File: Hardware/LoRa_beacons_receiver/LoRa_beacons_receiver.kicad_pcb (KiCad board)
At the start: 2 copper layers, 62.5 x 49 mm, 37 parts, among them J1 Conn_Coaxial, J2 USB_C_Receptacle_USB2.0_16P, J3 I2C_Display, J4 ST-Link, J5 1PPS_out, J6 Conn_02x09_Counter_Clockwise, Q1 DMG3402L, Q2 DMG3402L, SW1 RST_button, SW2 BOOT_button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

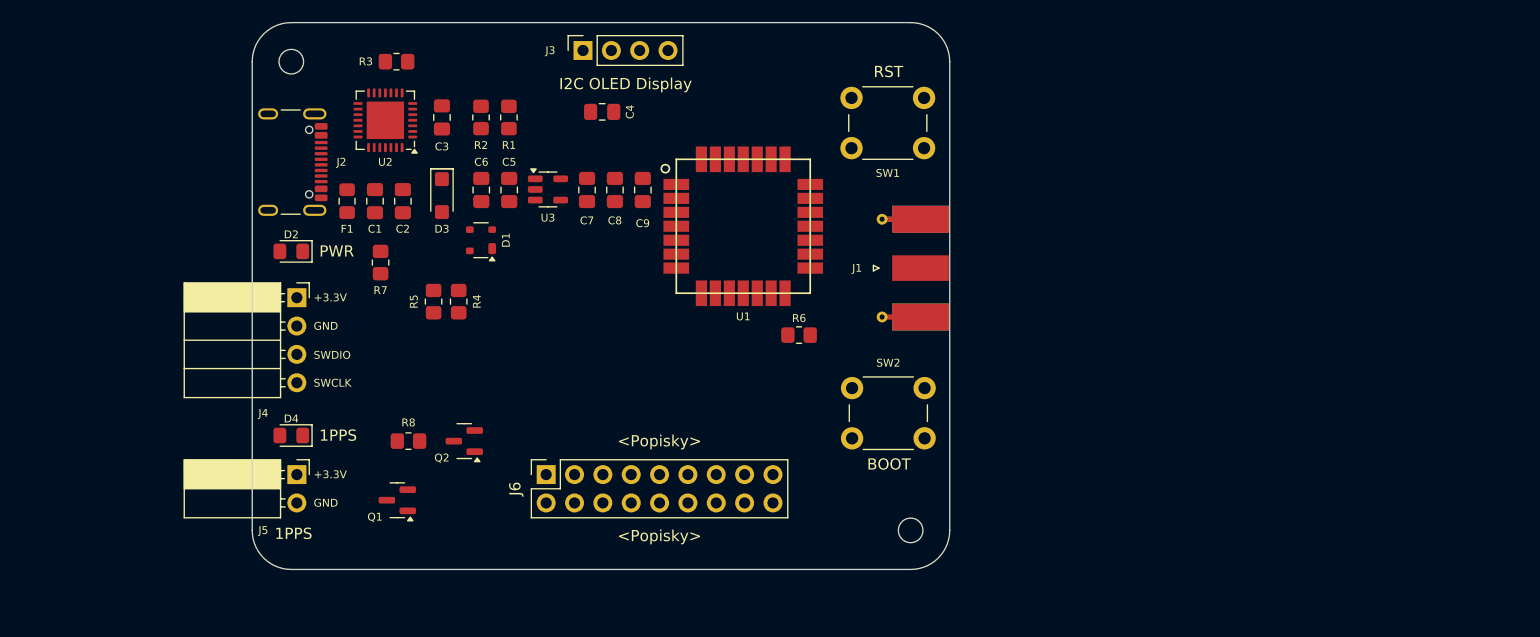
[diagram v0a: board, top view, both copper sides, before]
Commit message: Recommended KiCAD changes; PCB layout changes
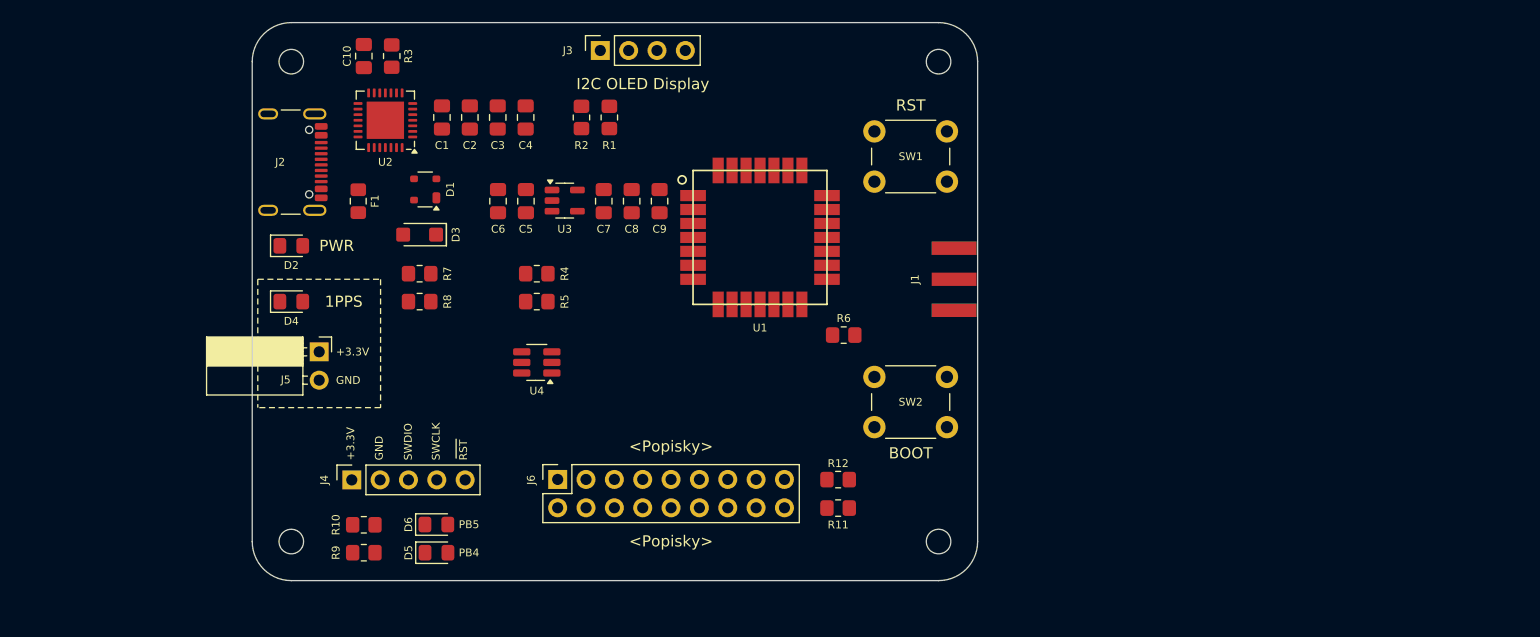
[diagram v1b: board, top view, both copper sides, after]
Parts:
- removed Q1, Q2: DMG3402L, Package_TO_SOT_SMD:SOT-23
- added C10: 100n, Capacitor_SMD:C_0805_2012Metric_Pad1.18x1.45mm_HandSolder, F.Cu at (110.0, 54.0)
- added D5: PB4, LED_SMD:LED_0805_2012Metric_Pad1.15x1.40mm_HandSolder, F.Cu at (116.5, 98.5)
- added D6: PB5, LED_SMD:LED_0805_2012Metric_Pad1.15x1.40mm_HandSolder, F.Cu at (116.5, 96.0)
- added H3: MountingHole, MountingHole:MountingHole_2.2mm_M2, F.Cu at (103.5, 97.5)
- added H4: MountingHole, MountingHole:MountingHole_2.2mm_M2, F.Cu at (161.5, 54.5)
- added R10: 56R, Resistor_SMD:R_0805_2012Metric_Pad1.20x1.40mm_HandSolder, F.Cu at (110.0, 96.0)
- added R11: 4.7k, Resistor_SMD:R_0805_2012Metric_Pad1.20x1.40mm_HandSolder, F.Cu at (152.5, 94.5)
- added R12: 4.7k, Resistor_SMD:R_0805_2012Metric_Pad1.20x1.40mm_HandSolder, F.Cu at (152.5, 92.0)
- added R9: 56R, Resistor_SMD:R_0805_2012Metric_Pad1.20x1.40mm_HandSolder, F.Cu at (110.0, 98.5)
- added U4: 74LVC1G175, Package_TO_SOT_SMD:SOT-23-6_Handsoldering, F.Cu at (125.5, 81.5)
- C1: value 1u -> 4.7u
- C2: value 100n -> 1u
- J1: footprint Connector_Coaxial:SMA_Molex_73251-1153_EdgeMount_Horizontal -> Connector_Coaxial_g:RF2-143-T-17-50-G
- J4: footprint Connector_PinSocket_2.54mm:PinSocket_1x04_P2.54mm_Horizontal -> Connector_PinSocket_2.54mm:PinSocket_1x05_P2.54mm_Vertical
- moved J4 17.1 mm to (108.9, 92.0), turned to 90 degrees
- moved R8 12.5 mm to (115.0, 76.0), turned to 180 degrees
- moved D4 12.0 mm to (103.5, 76.0), turned to 0 degrees
- moved SW1 11.4 mm to (162.2, 65.2), turned to 180 degrees
- moved J5 11.2 mm to (106.0, 80.5)
- moved C1 9.60 mm to (117.0, 59.5)
- moved C2 9.60 mm to (119.5, 59.5), turned to -90 degrees
- moved R5 9.25 mm to (125.5, 76.0), turned to 180 degrees
- moved R1 9.00 mm to (132.0, 59.5)
- moved R2 9.00 mm to (129.5, 59.5)
- moved R4 7.43 mm to (125.5, 73.5), turned to 0 degrees
- moved C4 6.88 mm to (124.5, 59.5), turned to -90 degrees
- moved J1 6.81 mm to (164.9, 74.0), turned to 90 degrees
- moved D1 6.76 mm to (115.5, 66.0)
- moved C3 5.00 mm to (122.0, 59.5)
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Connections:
- C1 pad 1: +5V -> GND
- C1 pad 2: GND -> +3.3V
- C2 pad 1: +5V -> +3.3V
- C3 pad 1: VDD -> +3.3V
- C4 pad 1: //DTR -> +3.3V
- C4 pad 2: RST -> GND
- D2 pad 1: /PWR_LED -> GND
- D2 pad 2: +3.3V -> /PWR_LED_A
- D4 pad 1: /PPS_LED -> GND
- D4 pad 2: +3.3V -> /PPS_LED_A
- J5 pad 1: +3.3V -> /PPS_OUT
- J5 pad 2: /PPS_OUT_MOS_D -> GND
- R3 pad 1: VDD -> +3.3V
- R3 pad 2: /USB-UART_RST -> /RST
- R7 pad 1: /PWR_LED -> +3.3V
- R7 pad 2: GND -> /PWR_LED_A
- R8 pad 1: /PPS_LED -> 1PPS_LED
- R8 pad 2: /PPS_LED_MOS_D -> /PPS_LED_A
- SW1 pad 1: RST -> /RST
- U1 pad 17: RST -> /RST
- U1 pad 23: 1PPS_OUT -> 1PPS_CLK
- U2 pad 6: VDD -> +3.3V
- U2 pad 7: +5V -> +3.3V
- U2 pad 9: /USB-UART_RST -> /RST
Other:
- board size 62.5 x 49 mm -> 65 x 50 mm
- board text added: "PB4"
- board text added: "PB5"

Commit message: Clenaup
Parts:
- J1: footprint Connector_Coaxial_g:RF2-143-T-17-50-G -> Connector_Coaxial_l:RF2-143-T-17-50-G_l
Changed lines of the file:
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@@
 		)
 		(embedded_fonts no)
-		(model "${KIPRJMOD}/symbols/STM32_module_l.pretty/STM32WLE5JC_3D.stp"
+		(model "${KIPRJMOD}/3dmodels/STM32WLE5JC_3D_l.stp"
 			(offset
 				(xyz 0 0 2.5)
 			)
 			(scale
-				(xyz 0.0385 0.0385 0.0385)
+				(xyz 0.0395 0.0395 0.0395)
 			)
 			(rotate
@@
 		)
 		(embedded_fonts no)
-		(model "${KIPRJMOD}/symbols/Diode_SMD_l.pretty/MBR130LSFT1G.stp"
+		(model "${KIPRJMOD}/3dmodels/MBR130LSFT1G_l.stp"
 			(offset
 				(xyz 0 0 0)
@@
 			)
 		)
-		(model "${KIPRJMOD}/symbols/Display_l.pretty/OLED_0_96INCH.step"
+		(model "${KIPRJMOD}/3dmodels/OLED_0_96INCH_l.step"
 			(offset
 				(xyz 0 -9.15 11.5)
@@
 		)
 	)
-	(footprint "Connector_Coaxial_g:RF2-143-T-17-50-G"
+	(footprint "Connector_Coaxial_l:RF2-143-T-17-50-G_l"
 		(layer "F.Cu")
 		(at 164.9 74 90)
 		(property "Reference" "J1"
-			(at 0 -5.5066 90)
+			(at -0.325 -6.635 90)
 			(layer "F.SilkS")
 			(effects
 				(font
-					(size 0.7 0.7)
-					(thickness 0.1)
+					(size 1 1)
+					(thickness 0.15)
 				)
 			)
@@
 		)
 		(embedded_fonts no)
-		(model "C:/Users/DELL_KM/Documents/KiCad/9.0/3dmodels/RF2-143-T-17-50-G.step"
+		(model "${KIPRJMOD}/3dmodels/RF2-143-T-17-50-G_l.step"
 			(offset
 				(xyz 0 0 0)

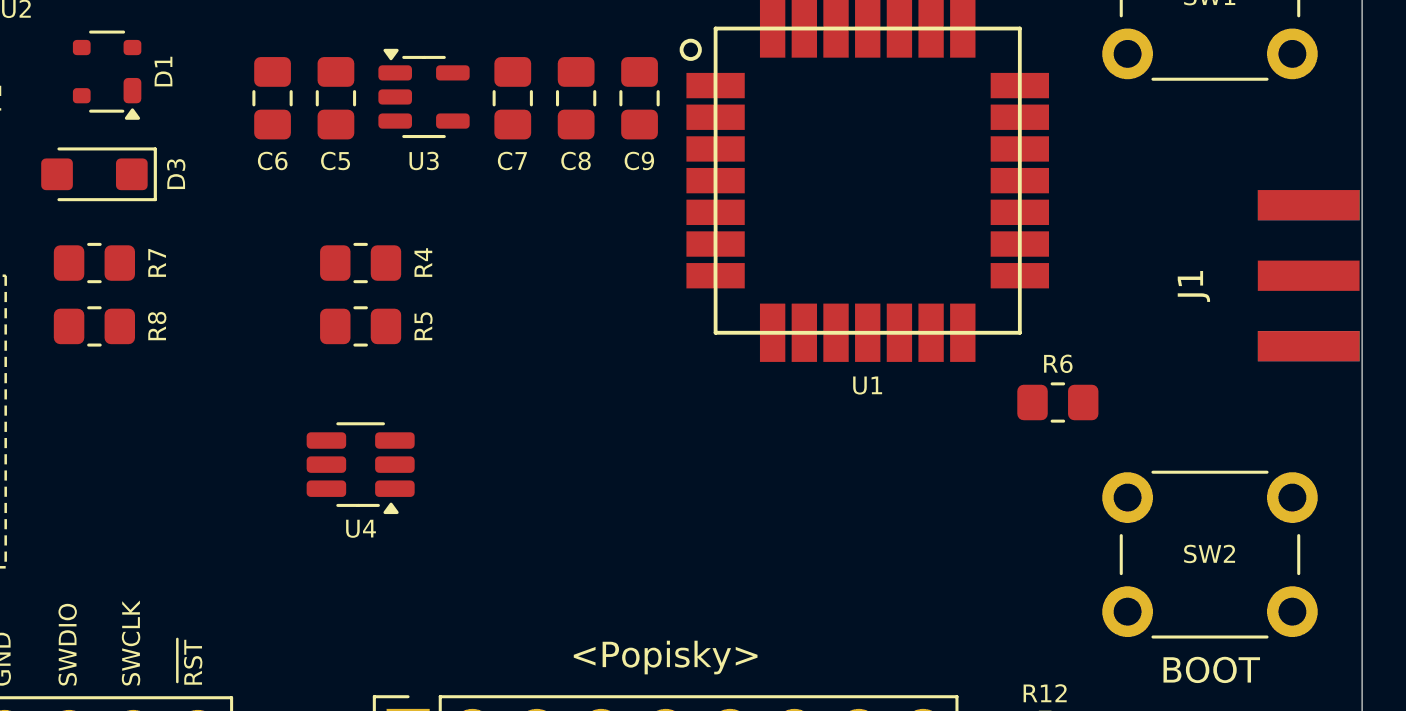
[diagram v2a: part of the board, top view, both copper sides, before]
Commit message: Minor schematic changes
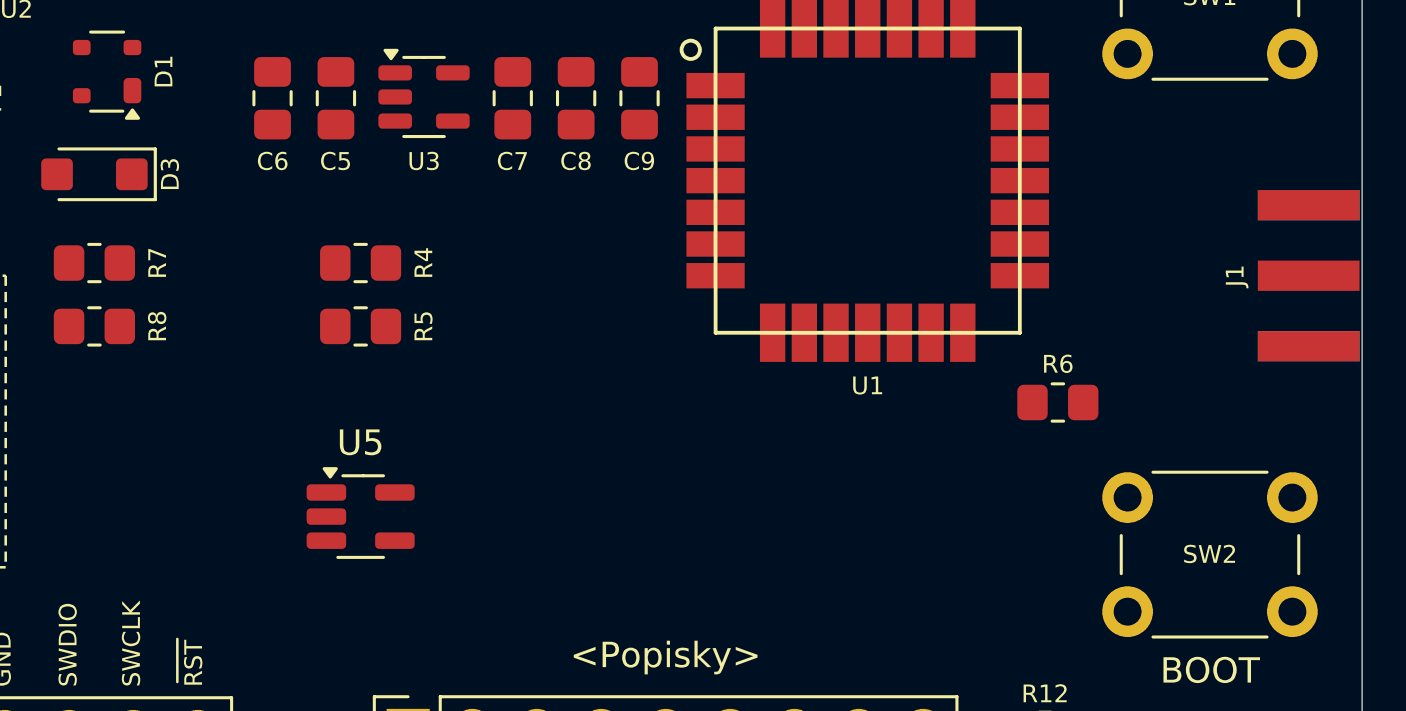
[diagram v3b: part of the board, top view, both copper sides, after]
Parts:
- removed U4: 74LVC1G175, Package_TO_SOT_SMD:SOT-23-6_Handsoldering
- added U5: 74LVC1G17, Package_TO_SOT_SMD:SOT-23-5_HandSoldering, F.Cu at (125.5, 83.5)
- D3: footprint Diode_SMD_l:SOD-123FL -> Diode_SMD_l:SOD-123FL_l
- U1: footprint STM32_module_l:STM32WLE5JC -> STM32_module_l:STM32WLE5JC_l
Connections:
- J6 pad 9: GND -> PB3
- R8 pad 1: 1PPS_LED -> /PPS_LED_A
- R8 pad 2: /PPS_LED_A -> 1PPS_CLK
- U1 pad 8: 1PPS_LED -> PB3

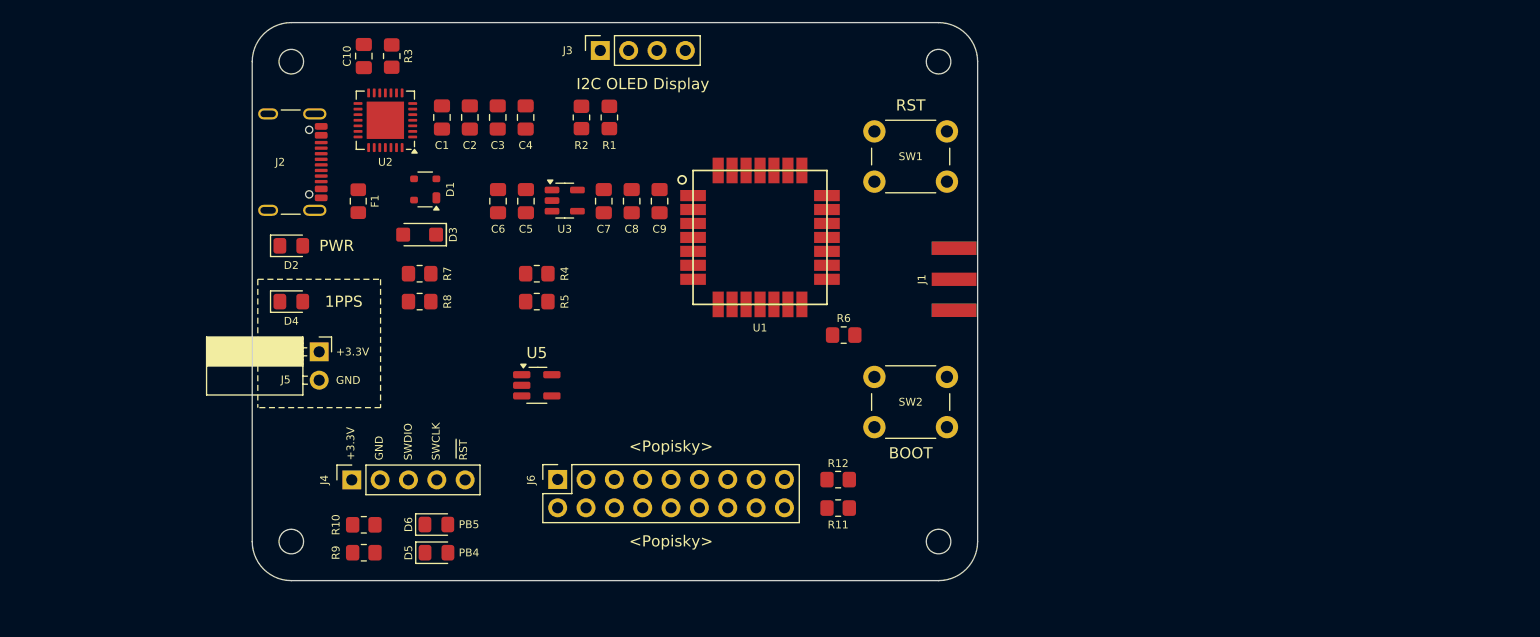
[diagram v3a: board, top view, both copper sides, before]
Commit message: Minor schematic changes; PCB WIP
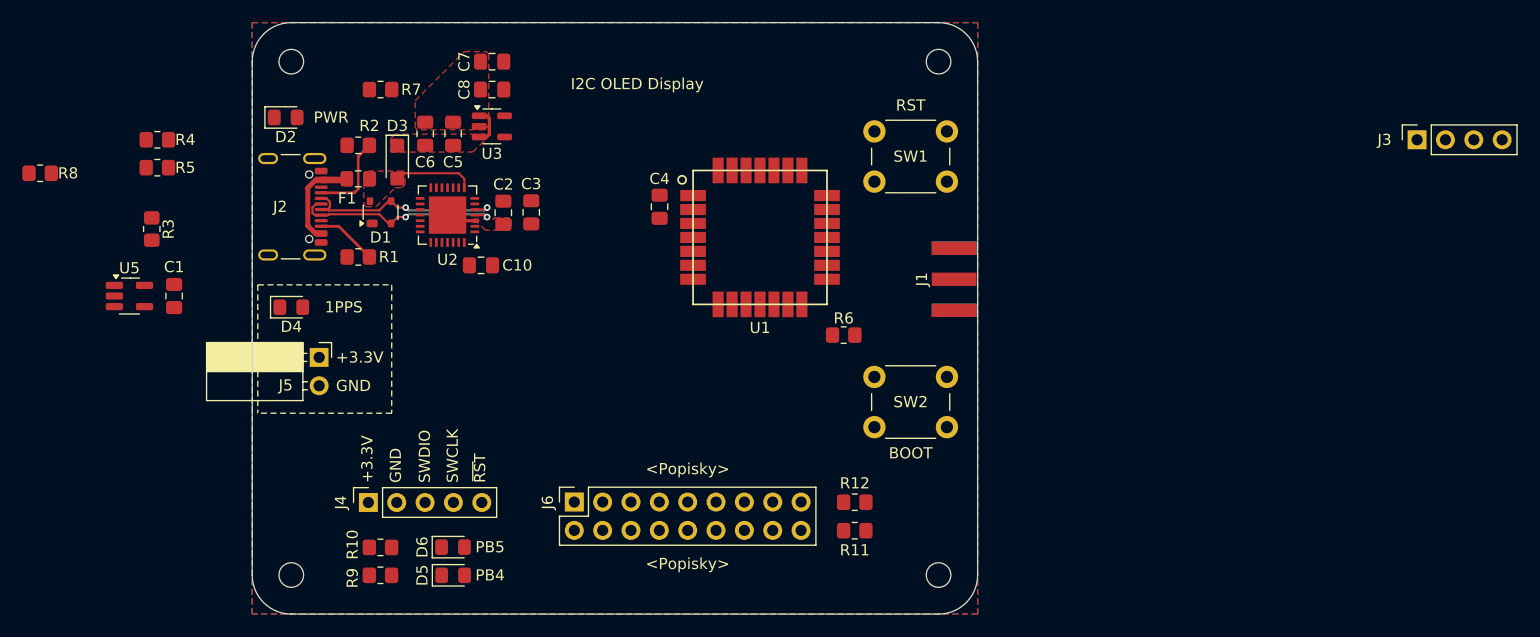
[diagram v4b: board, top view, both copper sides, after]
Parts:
- removed C9: 4.7u, Capacitor_SMD:C_0805_2012Metric_Pad1.18x1.45mm_HandSolder
- C1: value 4.7u -> 100n
- C4: value 100n -> 4.7u
- U1: value STM32WLE5JC -> Wio-E5
- moved J3 73.6 mm to (208.2, 61.5)
- moved U5 37.4 mm to (89.0, 75.5)
- moved R4 36.1 mm to (91.5, 61.5)
- moved R5 36.1 mm to (91.5, 64.0)
- moved R8 35.9 mm to (81.0, 64.5), turned to 0 degrees
- moved C1 28.8 mm to (93.0, 75.5), turned to -90 degrees
- moved R3 26.5 mm to (91.0, 69.5)
- moved R1 25.7 mm to (109.5, 72.0), turned to 180 degrees
- moved C10 21.5 mm to (120.5, 72.8), turned to 0 degrees
- moved R2 20.2 mm to (109.5, 62.0), turned to 180 degrees
- moved R7 16.9 mm to (111.5, 57.0)
- moved C7 16.0 mm to (121.5, 54.5), turned to 180 degrees
- moved C8 16.0 mm to (121.5, 57.0), turned to 180 degrees
- moved C4 14.4 mm to (136.5, 67.5)
- moved D2 11.5 mm to (103.0, 59.5)
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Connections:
- net /D+ renamed /USB_D_P
- net /D- renamed /USB_D_N
- C1 pad 1: GND -> +3.3V
- C1 pad 2: +3.3V -> GND
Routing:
- net /USB_D_N: track 0.00 -> 19.1 mm, vias 0 -> 2
- net /USB_D_P: track 0.00 -> 19.1 mm, vias 0 -> 2
- net /VBUS: track 0.00 -> 8.72 mm
- net /CC1: track 0.00 -> 7.78 mm
- net +5V: track 0.00 -> 7.24 mm
- net /CC2: track 0.00 -> 5.46 mm
- net /LDO_VIN: track 0.00 -> 3.43 mm
- net GND: track 0.00 -> 2.66 mm
- added copper zone on F.Cu, net +3.3V
- added copper zone on F.Cu, net +5V
- added copper zone on F.Cu, net /LDO_VIN
- added copper zone on B.Cu, net GND
- added copper zone on F.Cu, net GND
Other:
- board size 65 x 50 mm -> 65 x 53 mm

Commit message: First version of completely routed PCB
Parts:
- moved J3 76.1 mm to (132.5, 53.5)
- moved R4 42.2 mm to (129.2, 80.2)
- moved R5 42.0 mm to (129.2, 82.5)
- moved R8 37.5 mm to (116.0, 78.0), turned to -90 degrees
- moved R11 32.3 mm to (129.2, 75.8), turned to 180 degrees
- moved R3 31.1 mm to (121.5, 63.5), turned to 180 degrees
- moved R12 29.4 mm to (129.2, 78.0), turned to 180 degrees
- moved U5 29.2 mm to (117.5, 82.0), turned to 180 degrees
- moved C1 25.6 mm to (116.8, 85.0), turned to 0 degrees
- moved R6 4.07 mm to (150.0, 81.8), turned to 90 degrees
- moved J5 3.00 mm to (109.0, 81.0)
- moved R7 1.50 mm to (111.5, 55.5)
- moved R2 0.50 mm to (109.5, 62.5)
- moved C4 0.40 mm to (136.5, 67.1)
- moved J1 0.10 mm to (164.8, 74.0)
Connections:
- J6 pad 1: +5V -> PB0
- J6 pad 10: GND -> LPUART1_TX
- J6 pad 11: SPI2_MOSI -> SPI2_MISO
- J6 pad 12: SPI2_MISO -> SPI2_MOSI
- J6 pad 13: SPI2_NSS -> SPI2_SCK;BOOT
- J6 pad 14: SPI2_SCK;BOOT -> SPI2_NSS
- J6 pad 15: UART2_TX -> PB10
- J6 pad 16: UART2_RX -> PA9
- J6 pad 17: I2C2_SDA -> UART2_RX
- J6 pad 18: I2C2_SCL -> UART2_TX
- J6 pad 3: PB4 -> I2C2_SCL
- J6 pad 4: PB5 -> I2C2_SDA
- J6 pad 5: PB10 -> PB3
- J6 pad 6: PA9 -> PB4
- J6 pad 7: LPUART1_TX -> PB5
- J6 pad 8: LPUART1_RX -> GND
- J6 pad 9: PB3 -> LPUART1_RX
- U1 pad 28: unconnected-(U1-PB0-Pad28) -> PB0
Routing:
- net /RST: track 0.00 -> 89.2 mm, vias 0 -> 6
- net GND: track 2.66 -> 57.7 mm, vias 0 -> 18
- net I2C2_SDA: track 0.00 -> 52.4 mm, vias 0 -> 2
- net SPI2_SCK;BOOT: track 0.00 -> 51.8 mm, vias 0 -> 1
- net I2C2_SCL: track 0.00 -> 49.6 mm, vias 0 -> 2
- net 1PPS_CLK: track 0.00 -> 49.2 mm, vias 0 -> 2
- net PB4: track 0.00 -> 42.3 mm, vias 0 -> 1
- net SWDIO: track 0.00 -> 42.2 mm, vias 0 -> 1
- net PB5: track 0.00 -> 41.2 mm
- net PB0: track 0.00 -> 39.8 mm, vias 0 -> 1
- net SWCLK: track 0.00 -> 38.6 mm, vias 0 -> 1
- net SPI2_MOSI: track 0.00 -> 34.9 mm, vias 0 -> 1
- net PA9: track 0.00 -> 34.6 mm, vias 0 -> 1
- net SPI2_NSS: track 0.00 -> 33.9 mm, vias 0 -> 1
- net SPI2_MISO: track 0.00 -> 30.9 mm, vias 0 -> 1
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- added copper zone on B.Cu, net +3.3V
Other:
- board text added: "MISO2"
- board text added: "MOSI2"
- board text added: "NSS2"
- board text added: "PA9"
- board text added: "PB0"
- board text added: "PB10"
- board text added: "PB3"
- board text added: "PC0"
- board text added: "PC1"
- board text added: "RX2"
- board text added: "SCK2"
- board text added: "SCL2"
- board text added: "SDA2"
- board text added: "TX2"
- board text removed: "<Popisky>"

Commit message: Minor changes
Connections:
- net UART1_RX-USB renamed UART1_TX-USB_RX
- net UART1_TX-USB renamed UART1_RX-USB_TX
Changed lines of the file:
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@@
 	(net 34 "PB3")
 	(net 35 "1PPS_CLK")
-	(net 36 "UART1_TX-USB")
+	(net 36 "UART1_RX-USB_TX")
 	(net 37 "/TXD")
-	(net 38 "UART1_RX-USB")
+	(net 38 "UART1_TX-USB_RX")
 	(net 39 "/RXD")
 	(net 40 "/BOOT_button")
@@
 			(size 1 2.3)
 			(layers "F.Cu" "F.Mask" "F.Paste")
-			(net 36 "UART1_TX-USB")
+			(net 36 "UART1_RX-USB_TX")
 			(pinfunction "PB7")
 			(pintype "input")
@@
 			(size 1 2.3)
 			(layers "F.Cu" "F.Mask" "F.Paste")
-			(net 38 "UART1_RX-USB")
+			(net 38 "UART1_TX-USB_RX")
 			(pinfunction "PB6")
 			(pintype "input")
@@
 			(layers "F.Cu" "F.Mask" "F.Paste")
 			(roundrect_rratio 0.208333)
-			(net 36 "UART1_TX-USB")
+			(net 36 "UART1_RX-USB_TX")
 			(pintype "passive")
 		)
@@
 			(layers "F.Cu" "F.Mask" "F.Paste")
 			(roundrect_rratio 0.208333)
-			(net 38 "UART1_RX-USB")
+			(net 38 "UART1_TX-USB_RX")
 			(pintype "passive")
 		)

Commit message: Recommended changes
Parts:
- moved R4 3.54 mm to (132.6, 81.4)
- moved R5 3.53 mm to (132.6, 83.6)
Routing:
- net GND: track 57.7 -> 2.66 mm, vias 18 -> 87
- net +3.3V: track 2.38 -> 12.5 mm, vias 24 -> 0
- net /RXD: track 18.9 -> 22.7 mm, vias 0 -> 2
- net /TXD: track 16.0 -> 19.8 mm, vias 0 -> 2
- net UART1_TX-USB_RX: track 18.0 -> 15.1 mm
- net UART1_RX-USB_TX: track 14.8 -> 11.9 mm
- net /RST: track 89.2 -> 87.2 mm, vias 6 -> 5
- net 1PPS_CLK: track 49.2 -> 50.6 mm
- net SWCLK: track 38.6 -> 39.3 mm
- net I2C2_SDA: track 52.4 -> 51.8 mm
- removed copper zone on B.Cu, net +3.3V
